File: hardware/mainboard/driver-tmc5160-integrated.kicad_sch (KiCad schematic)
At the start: 32 parts, among them M6 Micro-Fit 3.0, U1 TMC5160A-TA

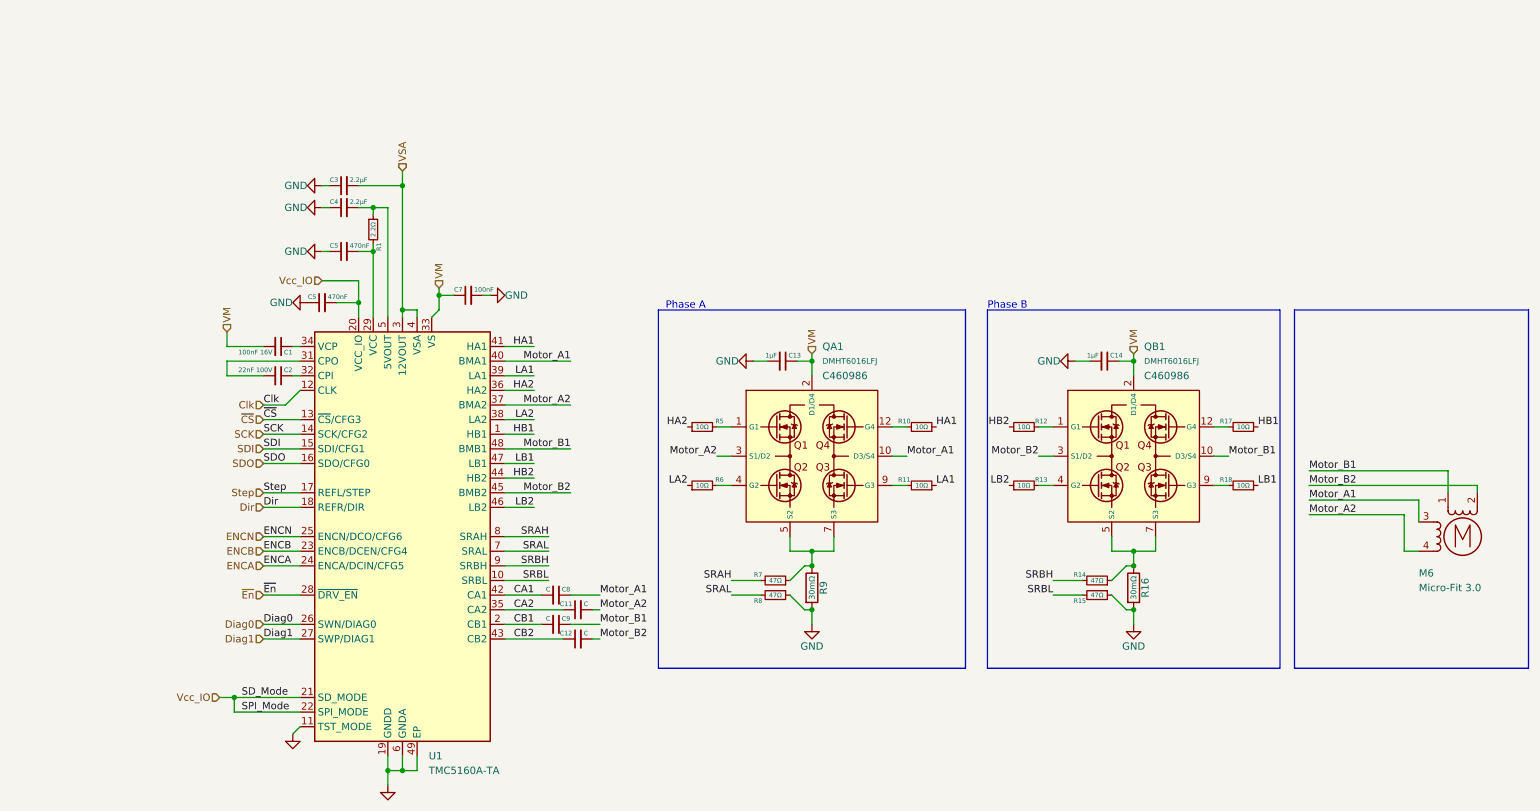
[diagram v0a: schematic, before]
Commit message: added fan / heater ports to mainboard, and footprints for switches, transistors, etc.
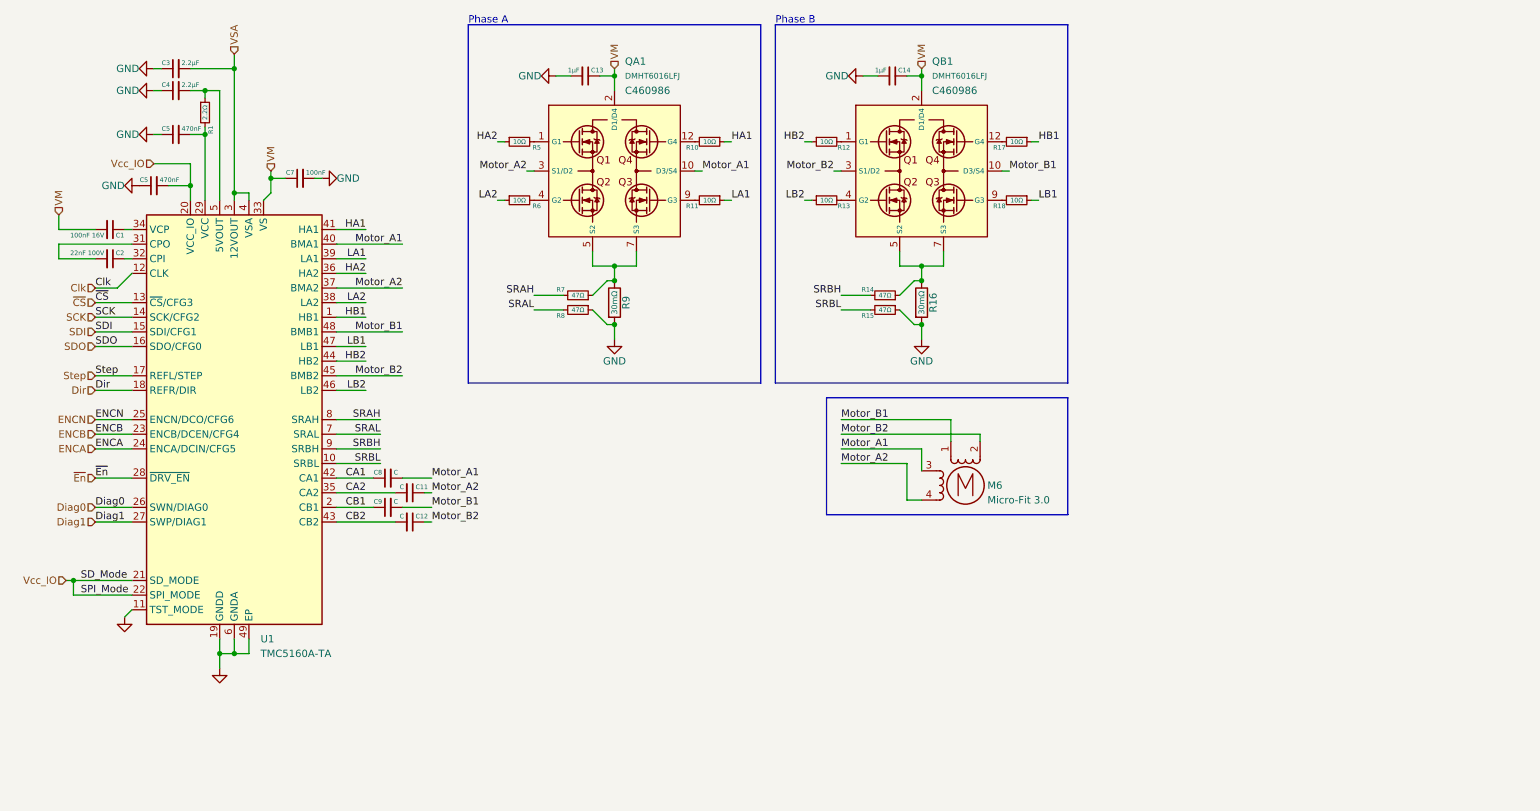
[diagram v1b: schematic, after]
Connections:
- net CA1: now also C8.1; no longer C8.2
- net CA2: now also C11.2; no longer C11.1
- net CB1: now also C9.1; no longer C9.2
- net CB2: now also C12.2; no longer C12.1
- net Motor_A1: now also C8.2; no longer C8.1
- net Motor_A2: now also C11.1; no longer C11.2
- net Motor_B1: now also C9.2; no longer C9.1
- net Motor_B2: now also C12.1; no longer C12.2
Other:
- company: (none) -> Meridi Engineering
- title: (none) -> Integrated TMCx160 Driver Block
- moved on the sheet: C1, C11, C12, C13, C14, C2, C3, C4, C5, C7, C8, C9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

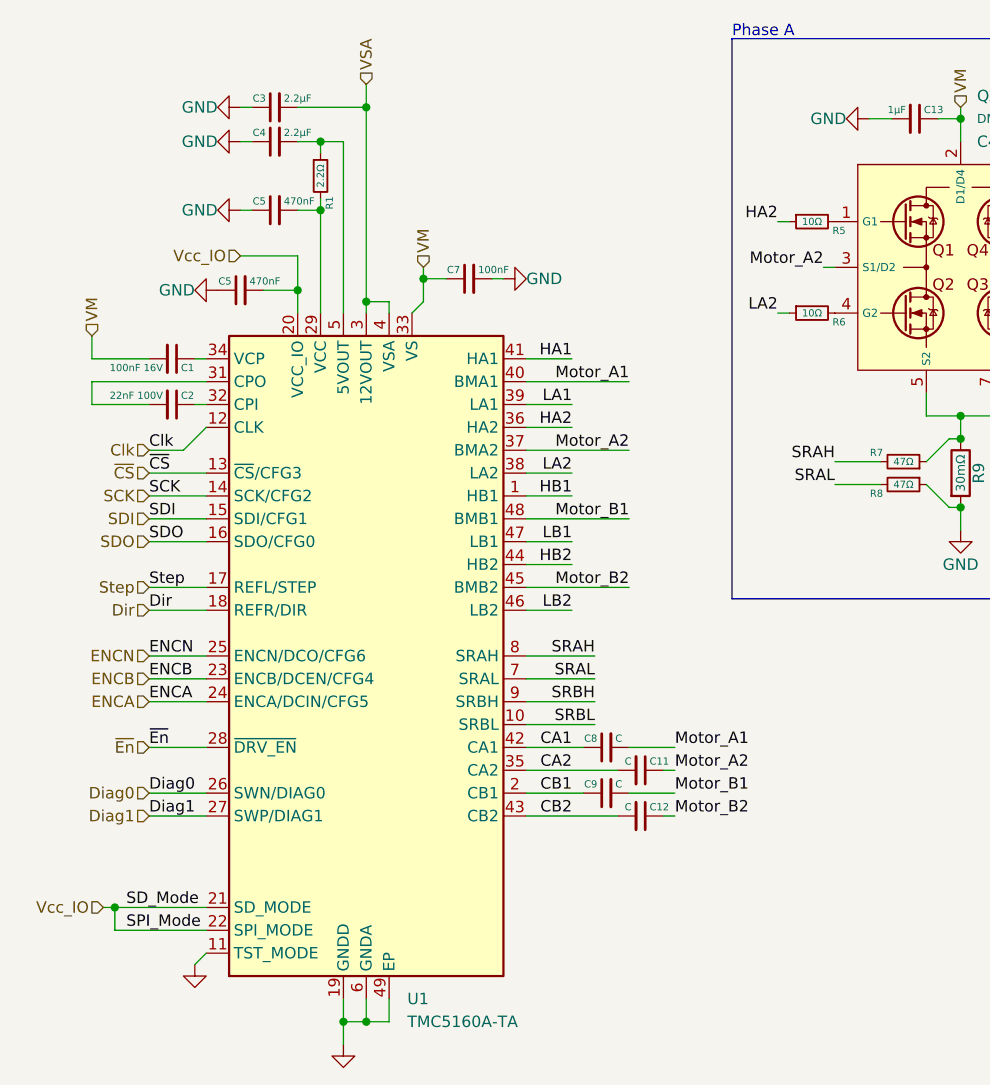
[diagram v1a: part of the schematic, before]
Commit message: saving mainboard, gonna tear out the entire thing and redo in 4-layer
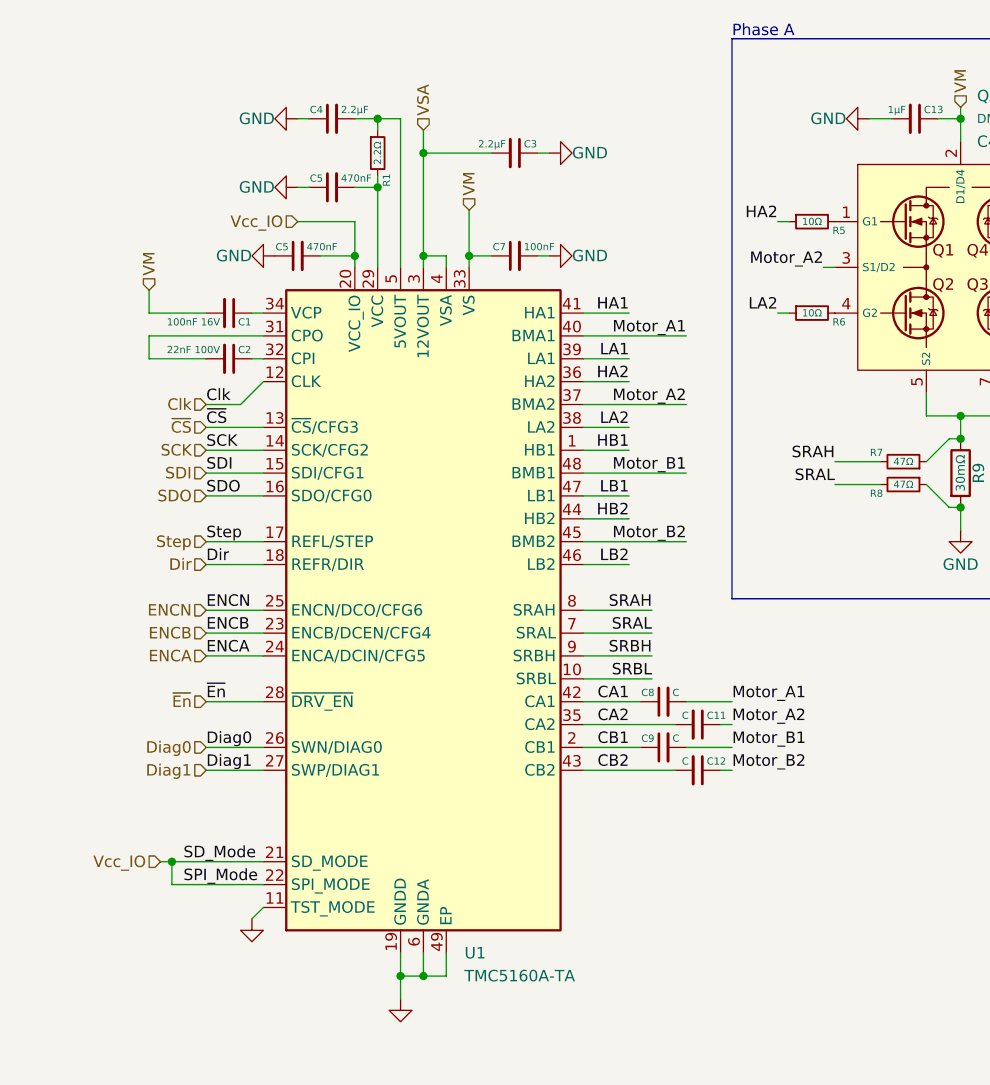
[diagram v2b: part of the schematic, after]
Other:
- moved on the sheet: C1, C11, C12, C2, C3, C4, C5, C7, C8, C9, R1, U1

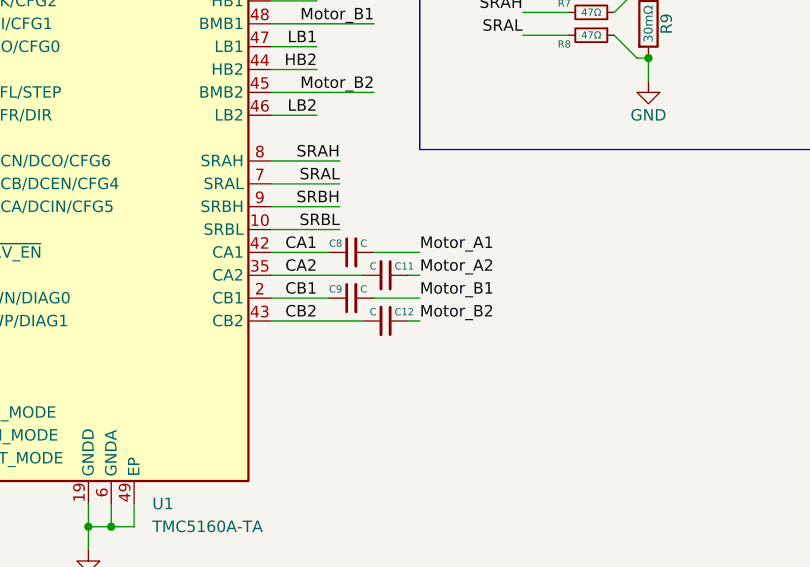
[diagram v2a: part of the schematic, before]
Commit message: further board edits, mostly done with power planes, heaters, fans, motor channels, starting work on microcontroller signals
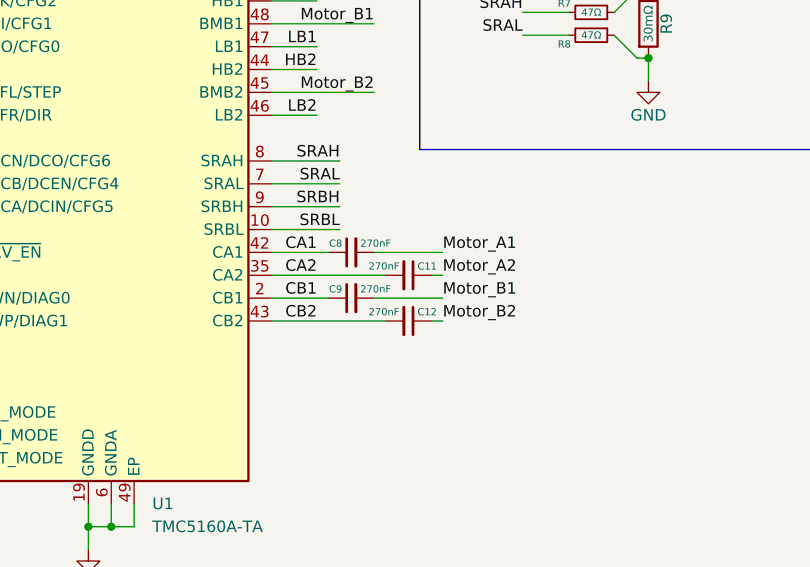
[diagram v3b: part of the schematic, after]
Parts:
- C11, C12, C8, C9: value C -> 270nF
- R1: footprint (none) -> AlphaLib:0402R
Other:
- moved on the sheet: C11, C12
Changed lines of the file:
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@@
     (stroke (width 0) (type default))
   )
-  (wire (pts (xy 88.9 91.44) (xy 90.17 91.44))
-    (stroke (width 0) (type default))
-  )
-  (wire (pts (xy 90.17 93.98) (xy 85.09 93.98))
+  (wire (pts (xy 91.44 91.44) (xy 92.71 91.44))
+    (stroke (width 0) (type default))
+  )
+  (wire (pts (xy 92.71 93.98) (xy 85.09 93.98))
     (stroke (width 0) (type default))
   )
@@
     (stroke (width 0) (type default))
   )
-  (wire (pts (xy 73.66 91.44) (xy 83.82 91.44))
+  (wire (pts (xy 73.66 91.44) (xy 86.36 91.44))
     (stroke (width 0) (type default))
   )
@@
     (stroke (width 0) (type default))
   )
-  (wire (pts (xy 83.82 96.52) (xy 73.66 96.52))
+  (wire (pts (xy 86.36 96.52) (xy 73.66 96.52))
     (stroke (width 0) (type default))
   )
@@
     (stroke (width 0) (type default))
   )
-  (wire (pts (xy 88.9 96.52) (xy 90.17 96.52))
+  (wire (pts (xy 91.44 96.52) (xy 92.71 96.52))
     (stroke (width 0) (type default))
   )
@@
     (stroke (width 0) (type default))
   )
-  (wire (pts (xy 90.17 88.9) (xy 85.09 88.9))
+  (wire (pts (xy 92.71 88.9) (xy 85.09 88.9))
     (stroke (width 0) (type default))
   )
@@
     (effects (font (size 1.27 1.27)) (justify left bottom))
   )
-  (label "Motor_A2" (at 90.17 91.44 0) (fields_autoplaced)
-    (effects (font (size 1.27 1.27)) (justify left bottom))
-  )
-  (label "Motor_B2" (at 90.17 96.52 0) (fields_autoplaced)
+  (label "Motor_A2" (at 92.71 91.44 0) (fields_autoplaced)
+    (effects (font (size 1.27 1.27)) (justify left bottom))
+  )
+  (label "Motor_B2" (at 92.71 96.52 0) (fields_autoplaced)
     (effects (font (size 1.27 1.27)) (justify left bottom))
   )
@@
     (effects (font (size 1.27 1.27)) (justify right bottom))
   )
-  (label "Motor_B1" (at 90.17 93.98 0) (fields_autoplaced)
+  (label "Motor_B1" (at 92.71 93.98 0) (fields_autoplaced)
     (effects (font (size 1.27 1.27)) (justify left bottom))
   )
@@
     (effects (font (size 1.27 1.27)) (justify right bottom))
   )
-  (label "Motor_A1" (at 90.17 88.9 0) (fields_autoplaced)
+  (label "Motor_A1" (at 92.71 88.9 0) (fields_autoplaced)
     (effects (font (size 1.27 1.27)) (justify left bottom))
   )
@@
     )
   )
-  (symbol (lib_id "Device:C_Small") (at 86.36 91.44 270) (unit 1)
-    (in_bom yes) (on_board yes) (dnp no)
-    (property "Reference" "C11" (at 87.36 90.44 90)
+  (symbol (lib_id "Device:C_Small") (at 88.9 91.44 270) (unit 1)
+    (in_bom yes) (on_board yes) (dnp no)
+    (property "Reference" "C11" (at 89.9 90.44 90)
       (effects (font (size 0.8 0.8)) (justify left))
     )
-    (property "Value" "C" (at 85.36 90.44 90)
+    (property "Value" "270nF" (at 87.9 90.44 90)
       (effects (font (size 0.8 0.8)) (justify right))
     )
-    (property "Footprint" "AlphaLib:0402C" (at 86.36 91.44 0)
-      (effects (font (size 1.27 1.27)) hide)
-    )
-    (property "Datasheet" "~" (at 86.36 91.44 0)
+    (property "Footprint" "AlphaLib:0402C" (at 88.9 91.44 0)
+      (effects (font (size 1.27 1.27)) hide)
+    )
+    (property "Datasheet" "~" (at 88.9 91.44 0)
       (effects (font (size 1.27 1.27)) hide)
     )
@@
       (effects (font (size 0.8 0.8)) (justify left))
     )
-    (property "Value" "C" (at 83.55 92.98 90)
+    (property "Value" "270nF" (at 83.55 92.98 90)
       (effects (font (size 0.8 0.8)) (justify right))
     )
@@
       (effects (font (size 0.8 0.8)) (justify left))
     )
-    (property "Value" "C" (at 83.55 87.9 90)
+    (property "Value" "270nF" (at 83.55 87.9 90)
       (effects (font (size 0.8 0.8)) (justify right))
     )
@@
     )
   )
-  (symbol (lib_id "Device:C_Small") (at 86.36 96.52 270) (unit 1)
-    (in_bom yes) (on_board yes) (dnp no)
-    (property "Reference" "C12" (at 87.36 95.52 90)
+  (symbol (lib_id "Device:C_Small") (at 88.9 96.52 270) (unit 1)
+    (in_bom yes) (on_board yes) (dnp no)
+    (property "Reference" "C12" (at 89.9 95.52 90)
       (effects (font (size 0.8 0.8)) (justify left))
     )
-    (property "Value" "C" (at 85.36 95.52 90)
+    (property "Value" "270nF" (at 87.9 95.52 90)
       (effects (font (size 0.8 0.8)) (justify right))
     )
-    (property "Footprint" "AlphaLib:0402C" (at 86.36 96.52 0)
-      (effects (font (size 1.27 1.27)) hide)
-    )
-    (property "Datasheet" "~" (at 86.36 96.52 0)
+    (property "Footprint" "AlphaLib:0402C" (at 88.9 96.52 0)
+      (effects (font (size 1.27 1.27)) hide)
+    )
+    (property "Datasheet" "~" (at 88.9 96.52 0)
       (effects (font (size 1.27 1.27)) hide)
     )
@@
       (effects (font (size 0.8 0.8)))
     )
-    (property "Footprint" "" (at 50.8 27.94 0)
-      (effects (font (size 1.27 1.27)) hide)
-    )
+    (property "Footprint" "AlphaLib:0402R" (at 50.8 27.94 0)
+      (effects (font (size 1.27 1.27)) hide)
+    )

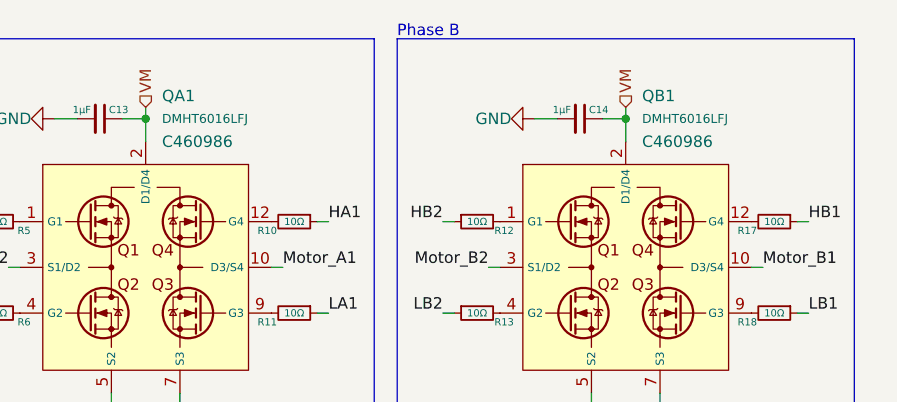
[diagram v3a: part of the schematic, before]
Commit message: redid mainboard, added probe wiring, replacing ncp chip with LM5160 for now
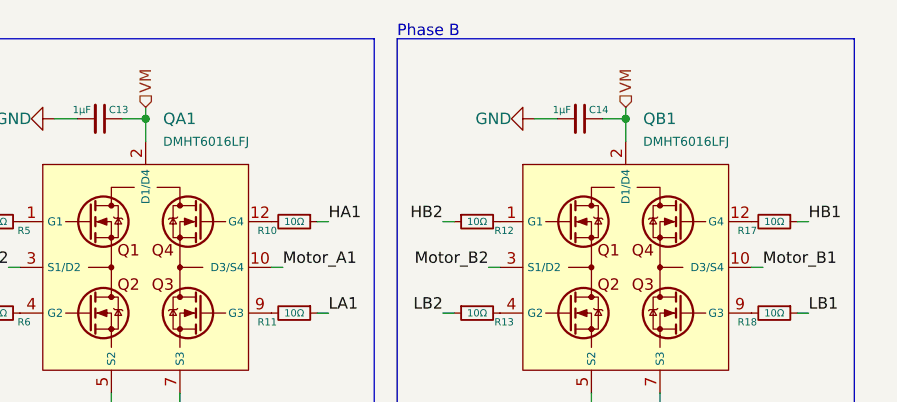
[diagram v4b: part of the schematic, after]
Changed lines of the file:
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@@
   (symbol (lib_id "tmc5160-driver:DMHT6016LFJ") (at 168.91 40.64 0) (unit 1)
     (in_bom yes) (on_board yes) (dnp no) (fields_autoplaced)
-    (property "Reference" "QB1" (at 170.7259 21.59 0)
+    (property "Reference" "QB1" (at 170.8497 24.13 0)
       (effects (font (size 1.27 1.27)) (justify left))
     )
-    (property "Value" "DMHT6016LFJ" (at 170.7259 24.13 0)
+    (property "Value" "DMHT6016LFJ" (at 170.8497 26.67 0)
       (effects (font (size 1 1)) (justify left))
     )
@@
     )
     (property "LCSC" "C460986" (at 170.7259 26.67 0)
-      (effects (font (size 1.27 1.27)) (justify left))
+      (effects (font (size 1.27 1.27)) (justify left) hide)
     )
     (pin "1")
@@
   (symbol (lib_id "tmc5160-driver:DMHT6016LFJ") (at 115.57 40.64 0) (unit 1)
     (in_bom yes) (on_board yes) (dnp no) (fields_autoplaced)
-    (property "Reference" "QA1" (at 117.3859 21.59 0)
+    (property "Reference" "QA1" (at 117.5097 24.13 0)
       (effects (font (size 1.27 1.27)) (justify left))
     )
-    (property "Value" "DMHT6016LFJ" (at 117.3859 24.13 0)
+    (property "Value" "DMHT6016LFJ" (at 117.5097 26.67 0)
       (effects (font (size 1 1)) (justify left))
     )
@@
     )
     (property "LCSC" "C460986" (at 117.3859 26.67 0)
-      (effects (font (size 1.27 1.27)) (justify left))
+      (effects (font (size 1.27 1.27)) (justify left) hide)
     )
     (pin "1")

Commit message: nearing first prototype woot! copyediting over entire board, fixed some mistakes
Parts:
- added C2: 47nF 100V/2, AlphaLib:0402C, symbol Device:C_Small
- added C7: 100nF 63V/2, AlphaLib:0402C, symbol Device:C_Small
- added R3: 10kΩ, AlphaLib:0402R, symbol Device:R_Small
- C11, C12, C8, C9: value 270nF -> 220nF
- C13, C14: value 1μF -> 1μF 63V; footprint Capacitor_SMD:C_0805_2012Metric -> Capacitor_SMD:C_1206_3216Metric
- C2: value 22nF 100V -> 47nF 100V/2
- C7: value 100nF -> 100nF 63V/2
- R16, R9: value 30mΩ -> 33mΩ; footprint Resistor_SMD:R_0805_2012Metric -> Resistor_SMD:R_1206_3216Metric
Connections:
- net GND: now also C7.2, R3.1; no longer C7.2
- net ~{En}: now also R3.2
- net at C2.2: now also C2.1; no longer U1.31 (CPO)
- new net: C2.2, U1.31 (CPO)
- new net: C7.1, C7.2
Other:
- moved on the sheet: C7
